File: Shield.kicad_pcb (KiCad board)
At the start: 2 copper layers, 68.8 x 53.6 mm, 33 parts, among them J1 Screw_Terminal_01x03, J2 Screw_Terminal_01x03, J3 Screw_Terminal_01x03, J4 Screw_Terminal_01x03, U1 MIC5219-3.3YM5, U2 MIC5219-3.3YM5, U3 MAX31865xAP, U4 MAX31865xAP, U5 MAX31865xAP, U6 MAX31865xAP

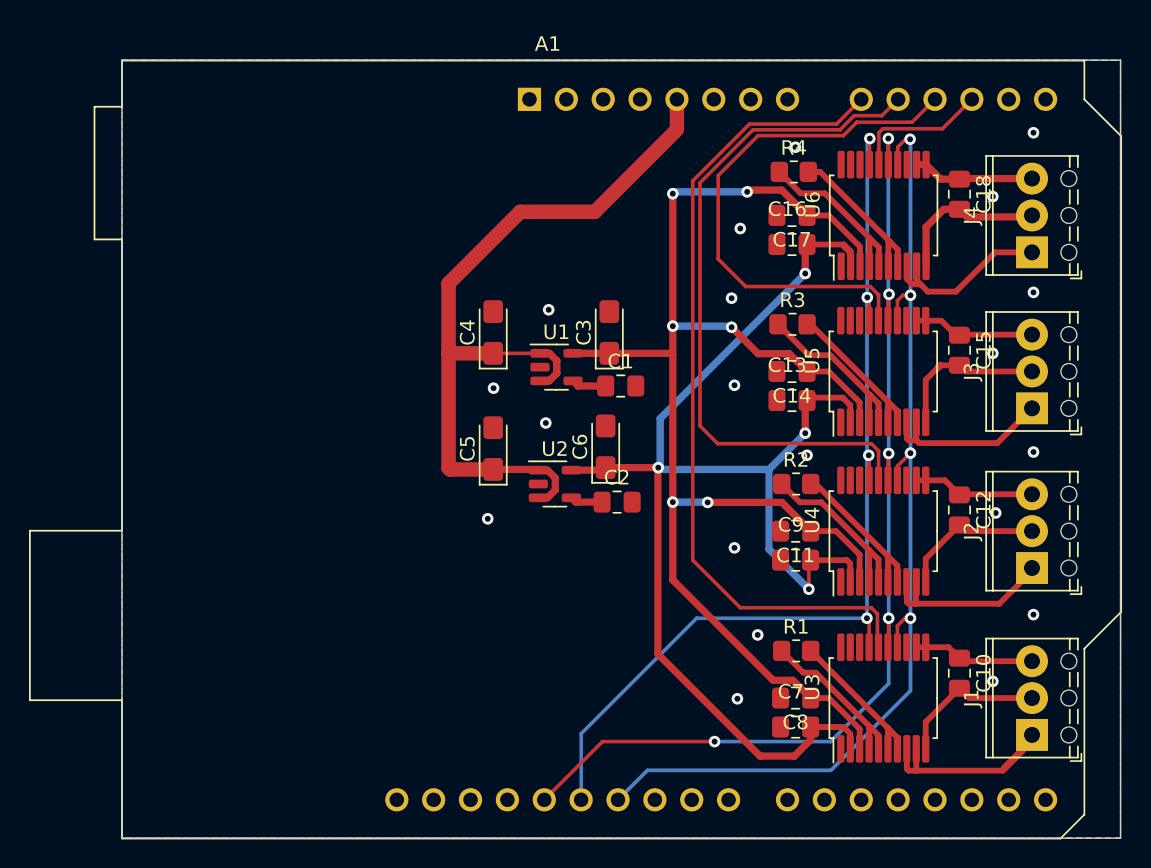
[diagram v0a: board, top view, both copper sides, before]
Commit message: Supprime le contour arduino qui fait plein d'erreur DRC
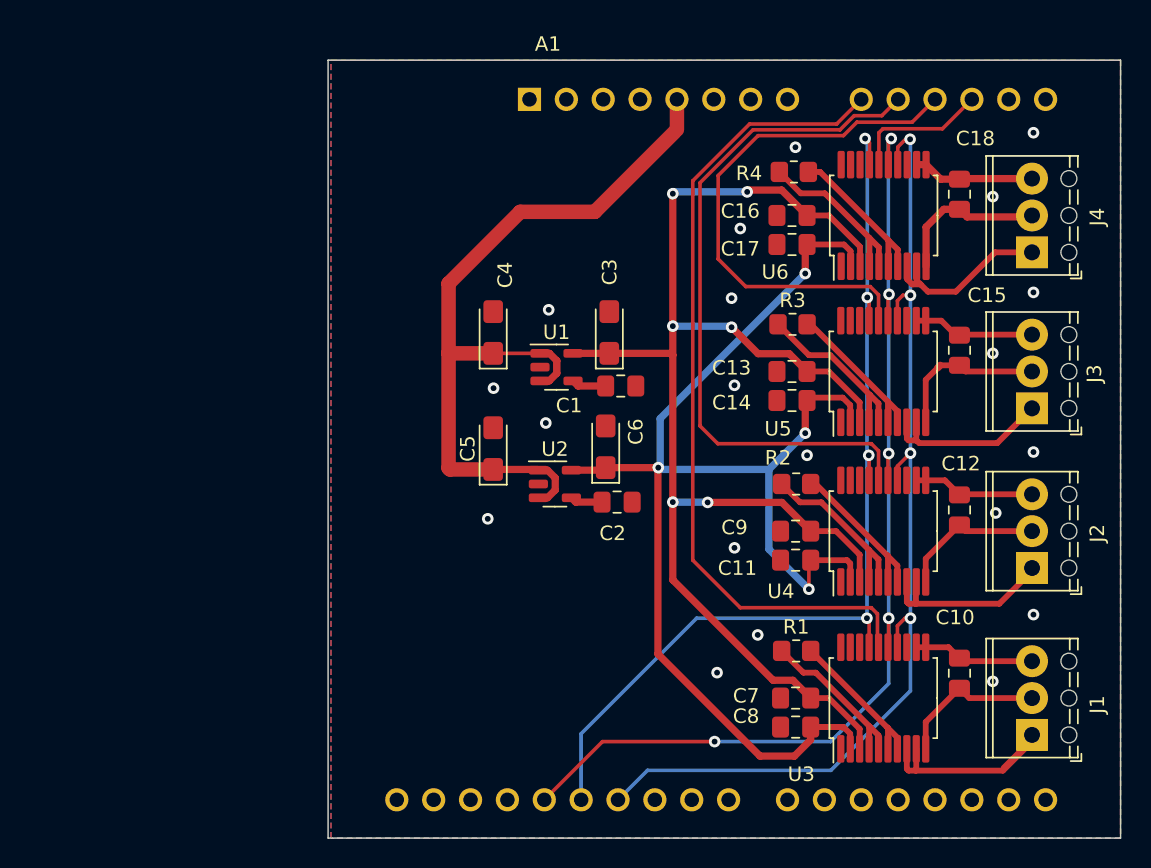
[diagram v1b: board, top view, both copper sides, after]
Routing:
- net +5V: track 64.5 -> 61.2 mm
- net +3.3V: track 105.3 -> 102.4 mm
- net Net-(R3-Pad1): track 14.3 -> 12.4 mm
- net Net-(C18-Pad2): track 11.7 -> 10.6 mm
- net Net-(J3-Pad1): track 13.7 -> 13.0 mm
- net Net-(R4-Pad2): track 12.0 -> 11.3 mm
- net Net-(U3-Pad8): track 15.9 -> 15.3 mm
- net Net-(C15-Pad2): track 12.5 -> 11.9 mm
- net Net-(C12-Pad2): track 10.7 -> 10.1 mm
- net Net-(R2-Pad2): track 11.6 -> 11.0 mm
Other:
- board size 68.8 x 53.6 mm -> 54.6 x 53.6 mm

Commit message: Passe l'empreinte en TSOP
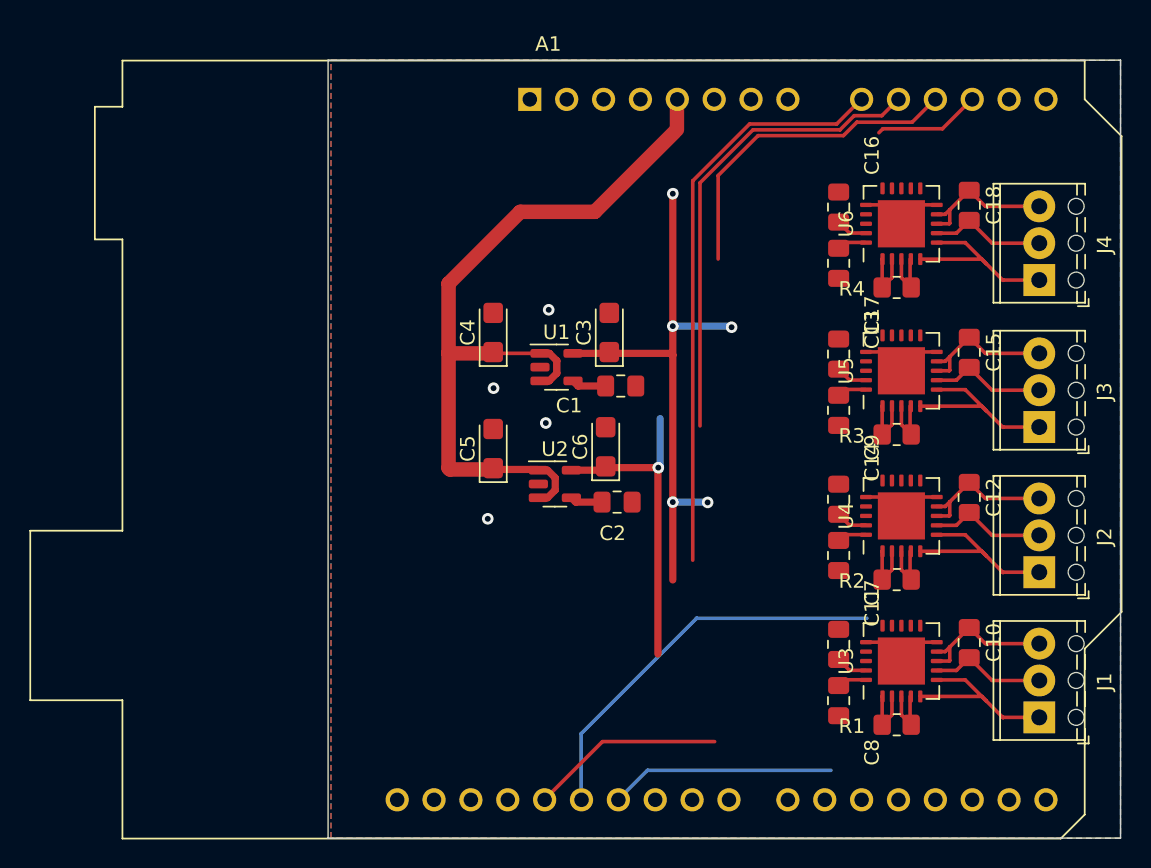
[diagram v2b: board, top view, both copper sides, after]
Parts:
- C3, C6: value 10µf -> 10uf; footprint Capacitor_Tantalum_SMD:CP_EIA-3216-18_Kemet-A_Pad1.58x1.35mm_HandSolder -> Capacitor_Tantalum_SMD:CP_EIA-3216-18_Kemet-A
- C4, C5: value 1µf -> 1uf; footprint Capacitor_Tantalum_SMD:CP_EIA-3216-18_Kemet-A_Pad1.58x1.35mm_HandSolder -> Capacitor_Tantalum_SMD:CP_EIA-3216-18_Kemet-A
- U3, U4, U5, U6: value MAX31865xAP -> MAX31865xTP; footprint Package_SO:SSOP-20_5.3x7.2mm_P0.65mm -> Package_DFN_QFN:TQFN-20-1EP_5x5mm_P0.65mm_EP3.25x3.25mm
- moved R4 10.7 mm to (139.2, 55.5)
- moved R3 10.4 mm to (139.2, 65.6)
- moved R2 9.56 mm to (139.2, 75.6)
- moved R1 8.59 mm to (139.2, 85.6)
- moved C7 6.42 mm to (135.2, 80.1), turned to -90 degrees
- moved C9 5.14 mm to (135.2, 70.1), turned to -90 degrees
- moved C17 4.60 mm to (135.2, 53.8), turned to -90 degrees
- moved C13 4.53 mm to (135.2, 60.1), turned to -90 degrees
- moved C14 4.18 mm to (135.2, 63.9), turned to -90 degrees
- moved C16 4.12 mm to (135.2, 49.9), turned to -90 degrees
- moved C11 3.40 mm to (135.2, 73.9), turned to -90 degrees
- moved C8 2.97 mm to (135.2, 83.9), turned to -90 degrees
- moved U3 2.84 mm to (139.5, 81.2)
- moved C10 2.22 mm to (144.2, 79.9)
- moved J4 1.98 mm to (149.0, 55.0)
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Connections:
- C10 pad 2: Net-(U3-Pad10) -> Net-(C10-Pad2)
- J1 pad 1: Net-(U3-Pad8) -> Net-(J1-Pad1)
- J1 pad 2: Net-(U3-Pad10) -> Net-(C10-Pad2)
- R1 pad 1: Net-(U3-Pad4) -> Net-(R1-Pad1)
- U3 pad 1: /MAX31865_1/DRDY -> Net-(R1-Pad1)
- U3 pad 10: Net-(U3-Pad10) -> GND
- U3 pad 11: Net-(C10-Pad1) -> /SPI2_MOSI
- U3 pad 12: Net-(C10-Pad1) -> /SPI2_SCK
- U3 pad 13: GND -> /CS_MAX1
- U3 pad 14: /SPI2_MOSI -> /SPI2_MISO
- U3 pad 15: /SPI2_SCK -> GND
- U3 pad 16: /CS_MAX1 -> GND
- U3 pad 17: /SPI2_MISO -> unconnected-(U3-Pad17)
- U3 pad 18: GND -> unconnected-(U3-Pad18)
- U3 pad 19: GND -> +3.3V
- U3 pad 2: +3.3V -> Net-(R1-Pad1)
- U3 pad 20: unconnected-(U3-Pad20) -> +3.3VA
- U3 pad 3: +3.3VA -> Net-(R1-Pad2)
- U3 pad 4: Net-(U3-Pad4) -> Net-(R1-Pad2)
- U3 pad 5: Net-(U3-Pad4) -> Net-(J1-Pad1)
- U3 pad 6: Net-(R1-Pad2) -> Net-(J1-Pad1)
- U3 pad 7: Net-(R1-Pad2) -> Net-(C10-Pad2)
- U3 pad 8: Net-(U3-Pad8) -> Net-(C10-Pad1)
- U3 pad 9: Net-(U3-Pad8) -> Net-(C10-Pad1)
- U4 pad 1: /MAX31865_2/DRDY -> Net-(R2-Pad1)
- U4 pad 10: Net-(C12-Pad2) -> GND
- U4 pad 11: Net-(C12-Pad1) -> /SPI2_MOSI
- U4 pad 12: Net-(C12-Pad1) -> /SPI2_SCK
- U4 pad 13: GND -> /CS_MAX2
- U4 pad 14: /SPI2_MOSI -> /SPI2_MISO
- U4 pad 15: /SPI2_SCK -> GND
- U4 pad 16: /CS_MAX2 -> GND
- U4 pad 17: /SPI2_MISO -> unconnected-(U4-Pad17)
- U4 pad 18: GND -> unconnected-(U4-Pad18)
- U4 pad 19: GND -> +3.3V
- U4 pad 2: +3.3V -> Net-(R2-Pad1)
- U4 pad 20: unconnected-(U4-Pad20) -> +3.3VA
- U4 pad 3: +3.3VA -> Net-(R2-Pad2)
- U4 pad 4: Net-(R2-Pad1) -> Net-(R2-Pad2)
- U4 pad 5: Net-(R2-Pad1) -> Net-(J2-Pad1)
- U4 pad 6: Net-(R2-Pad2) -> Net-(J2-Pad1)
- U4 pad 7: Net-(R2-Pad2) -> Net-(C12-Pad2)
- U4 pad 8: Net-(J2-Pad1) -> Net-(C12-Pad1)
- U4 pad 9: Net-(J2-Pad1) -> Net-(C12-Pad1)
- U5 pad 1: /MAX31865_3/DRDY -> Net-(R3-Pad1)
- U5 pad 10: Net-(C15-Pad2) -> GND
- U5 pad 11: Net-(C15-Pad1) -> /SPI2_MOSI
- U5 pad 12: Net-(C15-Pad1) -> /SPI2_SCK
- U5 pad 13: GND -> /CS_MAX3
- U5 pad 14: /SPI2_MOSI -> /SPI2_MISO
- U5 pad 15: /SPI2_SCK -> GND
- U5 pad 16: /CS_MAX3 -> GND
- U5 pad 17: /SPI2_MISO -> unconnected-(U5-Pad17)
- U5 pad 18: GND -> unconnected-(U5-Pad18)
- U5 pad 19: GND -> +3.3V
- U5 pad 2: +3.3V -> Net-(R3-Pad1)
- U5 pad 20: unconnected-(U5-Pad20) -> +3.3VA
- U5 pad 3: +3.3VA -> Net-(R3-Pad2)
- U5 pad 4: Net-(R3-Pad1) -> Net-(R3-Pad2)
- U5 pad 5: Net-(R3-Pad1) -> Net-(J3-Pad1)
- U5 pad 6: Net-(R3-Pad2) -> Net-(J3-Pad1)
- U5 pad 7: Net-(R3-Pad2) -> Net-(C15-Pad2)
- U5 pad 8: Net-(J3-Pad1) -> Net-(C15-Pad1)
- U5 pad 9: Net-(J3-Pad1) -> Net-(C15-Pad1)
- U6 pad 1: /MAX31865_4/DRDY -> Net-(R4-Pad1)
- U6 pad 10: Net-(C18-Pad2) -> GND
- U6 pad 11: Net-(C18-Pad1) -> /SPI2_MOSI
- U6 pad 12: Net-(C18-Pad1) -> /SPI2_SCK
- U6 pad 13: GND -> /CS_MAX4
- U6 pad 14: /SPI2_MOSI -> /SPI2_MISO
- U6 pad 15: /SPI2_SCK -> GND
- U6 pad 16: /CS_MAX4 -> GND
- U6 pad 17: /SPI2_MISO -> unconnected-(U6-Pad17)
- U6 pad 18: GND -> unconnected-(U6-Pad18)
- U6 pad 19: GND -> +3.3V
- U6 pad 2: +3.3V -> Net-(R4-Pad1)
- U6 pad 20: unconnected-(U6-Pad20) -> +3.3VA
- U6 pad 3: +3.3VA -> Net-(R4-Pad2)
- U6 pad 4: Net-(R4-Pad1) -> Net-(R4-Pad2)
- U6 pad 5: Net-(R4-Pad1) -> Net-(J4-Pad1)
- U6 pad 6: Net-(R4-Pad2) -> Net-(J4-Pad1)
- U6 pad 7: Net-(R4-Pad2) -> Net-(C18-Pad2)
- U6 pad 8: Net-(J4-Pad1) -> Net-(C18-Pad1)
- U6 pad 9: Net-(J4-Pad1) -> Net-(C18-Pad1)
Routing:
- net +3.3V: track 102.4 -> 30.9 mm, vias 4 -> 1
- net /SPI2_SCK: track 72.3 -> 13.4 mm, vias 5 -> 0
- net /SPI2_MOSI: track 70.8 -> 15.5 mm, vias 4 -> 0
- net +3.3VA: track 100.7 -> 48.2 mm, vias 6 -> 5
- net /SPI2_MISO: track 68.1 -> 27.5 mm, vias 4 -> 0
- net GND: track 0.00 -> 23.8 mm, vias 20 -> 4
- net /CS_MAX1: track 56.6 -> 40.1 mm
- net Net-(U3-Pad8): track 15.3 -> 0.00 mm
- net /CS_MAX2: track 47.8 -> 32.8 mm
- net Net-(R1-Pad2): track 18.7 -> 4.23 mm
- net /CS_MAX3: track 36.7 -> 22.9 mm
- net Net-(J1-Pad1): track 0.00 -> 12.8 mm
- net Net-(U3-Pad4): track 11.6 -> 0.00 mm
- net Net-(U3-Pad10): track 10.4 -> 0.00 mm
- net Net-(R2-Pad1): track 14.3 -> 4.16 mm
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
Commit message: Passe l'empreinte en TSOP
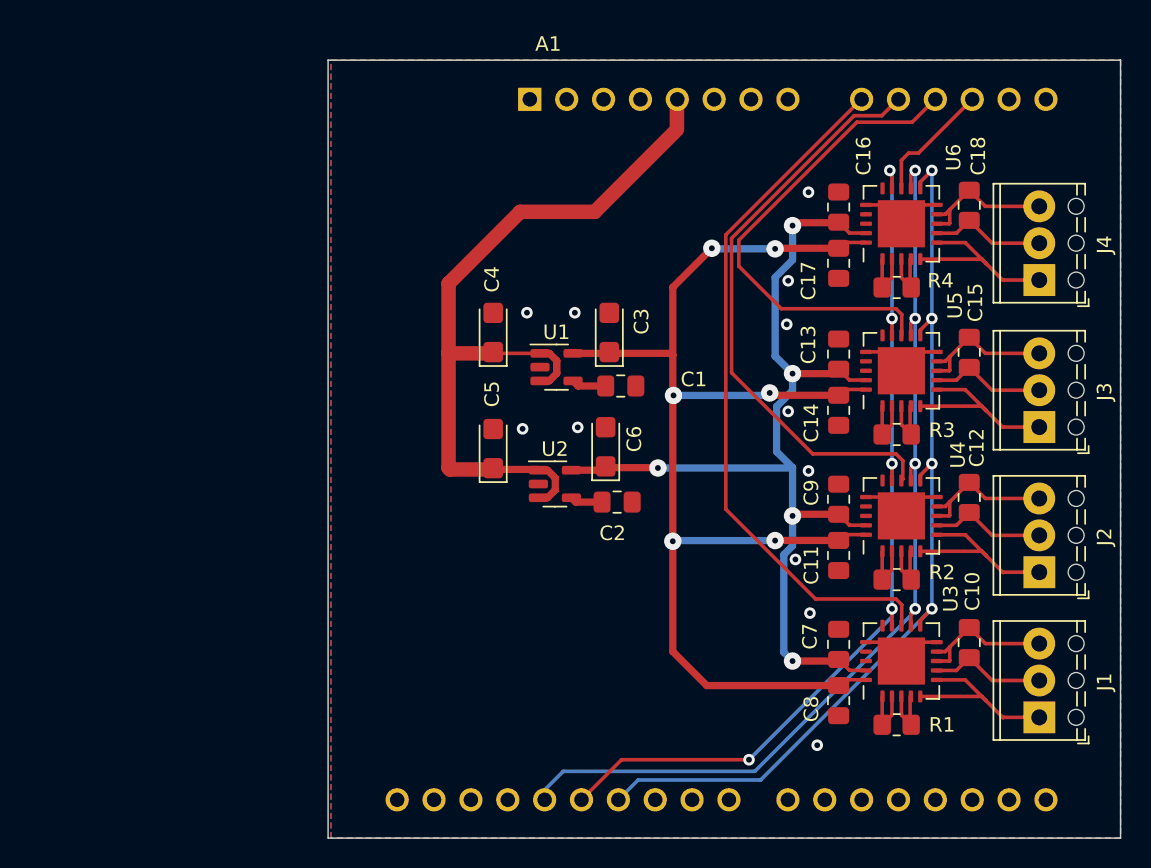
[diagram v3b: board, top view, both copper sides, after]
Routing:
- net /SPI2_SCK: track 13.4 -> 66.9 mm, vias 0 -> 4
- net /SPI2_MOSI: track 15.5 -> 63.3 mm, vias 0 -> 4
- net +3.3VA: track 48.2 -> 87.1 mm, vias 5 -> 6
- net +3.3V: track 30.9 -> 68.5 mm, vias 1 -> 5
- net /SPI2_MISO: track 27.5 -> 62.2 mm, vias 0 -> 5
- net GND: track 23.8 -> 9.10 mm, vias 4 -> 12
- net /CS_MAX3: track 22.9 -> 33.4 mm
- net /CS_MAX1: track 40.1 -> 48.4 mm
- net /CS_MAX2: track 32.8 -> 40.4 mm
- net /CS_MAX4: track 7.36 -> 8.55 mm
